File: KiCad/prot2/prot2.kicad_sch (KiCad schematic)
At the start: 1 part, among them Q1 Q_Photo_NPN

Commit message: 回路図仮完成
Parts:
- added C1, C10, C2, C3, C4, C5, C6, C7, C8, C9: C, symbol Device:C
- added C11, C12, C13: C_Polarized_Small_US, symbol Device:C_Polarized_Small_US
- added D1, D10, D11, D12, D13, D14, D15, D16, D17, D18, D19, D2, D20, D21, D22, D23, D24, D25, D26, D27, D28, D29, D3, D30, D31, D32, D4, D5, D6, D7, D8, D9: LED, symbol Device:LED
- added D33: D_Schottky, symbol Device:D_Schottky
- added J1: Conn_01x02_Socket, symbol Connector:Conn_01x02_Socket
- added J2: LED_SW, symbol Connector_Generic:Conn_01x03
- added J3: Conn_01x04_Socket, symbol Connector:Conn_01x04_Socket
- added Q10, Q11, Q12, Q13, Q14, Q15, Q16, Q17, Q18, Q19, Q2, Q20, Q21, Q22, Q23, Q24, Q25, Q26, Q27, Q28, Q29, Q3, Q30, Q31, Q32, Q4, Q5, Q6, Q7, Q8, Q9: Q_Photo_NPN, symbol Device:Q_Photo_NPN
- added RP2040_Zero1, RP2040_Zero2: ~, RP2040_Zero:名称未設定, symbol RP2040-zero:RP2040_Zero
- added RV1: R_Potentiometer_Trim, symbol Device:R_Potentiometer_Trim
- added Rc1, Rc10, Rc11, Rc12, Rc13, Rc14, Rc15, Rc16, Rc17, Rc18, Rc19, Rc2, Rc20, Rc21, Rc22, Rc23, Rc24, Rc25, Rc26, Rc27, Rc28, Rc29, Rc3, Rc30, Rc31, Rc32, Rc4, Rc5, Rc6, Rc7, Rc8, Rc9, Rl1, Rl10, Rl11, Rl12, Rl13, Rl14, Rl15, Rl16, Rl17, Rl18, Rl19, Rl2, Rl20, Rl21, Rl22, Rl23, Rl24, Rl25, Rl26, Rl27, Rl28, Rl29, Rl3, Rl30, Rl31, Rl32, Rl4, Rl5, Rl6, Rl7, Rl8, Rl9, Rs1, Rs10, Rs11, Rs12, Rs13, Rs14, Rs15, Rs16, Rs17, Rs18, Rs19, Rs2, Rs20, Rs21, Rs22, Rs23, Rs24, Rs25, Rs26, Rs27, Rs28, Rs29, Rs3, Rs30, Rs31, Rs32, Rs4, Rs5, Rs6, Rs7, Rs8, Rs9: R, symbol Device:R
- added U1, U2, U3, U4, U5, U6, U7, U8: LM339, symbol Comparator:LM339
- Q1: footprint ALS-PT19-315C:ALS-PT19-315C -> (none)
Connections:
- net VCC: now reaches Q1.1 (C)
- net VCC: now also C1.1, C2.1, C3.1, C4.1, C5.1, C6.1, C7.1, C8.1, D33.1 (K), Q10.1 (C), Q11.1 (C), Q12.1 (C), Q13.1 (C), Q14.1 (C), Q15.1 (C), Q16.1 (C), Q17.1 (C), Q18.1 (C), Q19.1 (C), Q2.1 (C), Q20.1 (C), Q21.1 (C), Q22.1 (C), Q23.1 (C), Q24.1 (C), Q25.1 (C), Q26.1 (C), Q27.1 (C), Q28.1 (C), Q29.1 (C), Q3.1 (C), Q30.1 (C), Q31.1 (C), Q32.1 (C), Q4.1 (C), Q5.1 (C), Q6.1 (C), Q7.1 (C), Q8.1 (C), Q9.1 (C), RP2040_Zero1.21 (3V3), RP2040_Zero2.21 (3V3), RV1.1, Rc1.1, Rc10.1, Rc11.1, Rc12.1, Rc13.1, Rc14.1, Rc15.1, Rc16.1, Rc17.1, Rc18.1, Rc19.1, Rc2.1, Rc20.1, Rc21.1, Rc22.1, Rc23.1, Rc24.1, Rc25.1, Rc26.1, Rc27.1, Rc28.1, Rc29.1, Rc3.1, Rc30.1, Rc31.1, Rc32.1, Rc4.1, Rc5.1, Rc6.1, Rc7.1, Rc8.1, Rc9.1, U1.3 (V+), U2.3 (V+), U3.3 (V+), U4.3 (V+), U5.3 (V+), U6.3 (V+), U7.3 (V+), U8.3 (V+)
- net at Q1.2 (E): now also Rs1.1, U1.4 (-)
- new net: Q4.2 (E), Rs4.1, U1.8 (-)
- new net: Q16.2 (E), Rs16.1, U4.8 (-)
- new net: D27.1 (K), Rl27.1
- new net: D12.1 (K), Rl12.1
- new net: D32.1 (K), Rl32.1
- new net: Q7.2 (E), Rs7.1, U2.10 (-)
- new net: D24.1 (K), Rl24.1
- new net: Q32.2 (E), Rs32.1, U8.8 (-)
- new net: Q31.2 (E), Rs31.1, U7.8 (-)
- new net: D3.1 (K), Rl3.1
- new net: Q14.2 (E), Rs14.1, U4.6 (-)
- new net: D28.1 (K), Rl28.1
- new net: D4.1 (K), Rl4.1
- new net: D30.1 (K), Rl30.1
- new net: Q27.2 (E), Rs27.1, U7.10 (-)
- new net: Q13.2 (E), Rs13.1, U4.4 (-)
- new net: Q12.2 (E), Rs12.1, U3.8 (-)
- new net: Q29.2 (E), Rs29.1, U5.8 (-)
- new net: D9.1 (K), Rl9.1
- new net: D14.1 (K), Rl14.1
- new net: Q8.2 (E), Rs8.1, U2.8 (-)
- new net: Q10.2 (E), Rs10.1, U3.6 (-)
- new net: D7.1 (K), Rl7.1
- new net: Q5.2 (E), Rs5.1, U2.4 (-)
- new net: Q9.2 (E), Rs9.1, U3.4 (-)
- new net: Q23.2 (E), Rs23.1, U7.6 (-)
- new net: D17.1 (K), Rl17.1
- new net: D18.1 (K), Rl18.1
- new net: Q19.2 (E), Rs19.1, U7.4 (-)
- new net: D11.1 (K), Rl11.1
- new net: Q24.2 (E), Rs24.1, U8.6 (-)
- new net: Q22.2 (E), Rs22.1, U6.6 (-)
- new net: Q3.2 (E), Rs3.1, U1.10 (-)
- new net: D31.1 (K), Rl31.1
- new net: D25.1 (K), Rl25.1
- new net: Q2.2 (E), Rs2.1, U1.6 (-)
- new net: D10.1 (K), Rl10.1
- new net: D8.1 (K), Rl8.1
- new net: D21.1 (K), Rl21.1
- new net: D16.1 (K), Rl16.1
- new net: D6.1 (K), Rl6.1
- new net: Q11.2 (E), Rs11.1, U3.10 (-)
- new net: Q21.2 (E), Rs21.1, U5.6 (-)
- new net: Q26.2 (E), Rs26.1, U6.10 (-)
- new net: Q20.2 (E), Rs20.1, U8.4 (-)
- new net: RP2040_Zero1., RP2040_Zero1.8 (7)
- new net: Q15.2 (E), Rs15.1, U4.10 (-)
- new net: D13.1 (K), Rl13.1
- new net: D19.1 (K), Rl19.1
- new net: Q18.2 (E), Rs18.1, U6.4 (-)
- new net: D22.1 (K), Rl22.1
- new net: Q6.2 (E), Rs6.1, U2.6 (-)
- new net: D26.1 (K), Rl26.1
- new net: D15.1 (K), Rl15.1
- new net: Q30.2 (E), Rs30.1, U6.8 (-)
- new net: Q25.2 (E), Rs25.1, U5.10 (-)
- new net: Q17.2 (E), Rs17.1, U5.4 (-)
- new net: Q28.2 (E), Rs28.1, U8.10 (-)
- new net: D1.1 (K), Rl1.1
- new net: D23.1 (K), Rl23.1
- new net: D2.1 (K), Rl2.1
- new net: D29.1 (K), Rl29.1
- new net: RP2040_Zero2., RP2040_Zero2.8 (7)
- new net: D20.1 (K), Rl20.1
- new net: D5.1 (K), Rl5.1
- new net 1: Rc1.2, U1.2
- new net 10: Rc10.2, U3.1
- new net 11: Rc11.2, U3.13
- new net 12: Rc12.2, U3.14
- new net 13: Rc13.2, U4.2
- new net 14: Rc14.2, U4.1
- new net 15: Rc15.2, U4.13
- new net 16: Rc16.2, U4.14
- new net 17: Rc17.2, U5.2
- new net 18: Rc18.2, U5.1
- new net 19: Rc19.2, U5.13
- new net 2: Rc2.2, U1.1
- new net 20: Rc20.2, U5.14
- new net 21: Rc21.2, U6.2
- new net 22: Rc22.2, U6.1
- new net 23: Rc23.2, U6.13
- new net 24: Rc24.2, U6.14
- new net 25: Rc25.2, U7.2
- new net 26: Rc26.2, U7.1
- new net 27: Rc27.2, U7.13
- new net 28: Rc28.2, U7.14
- new net 29: Rc29.2, U8.2
- new net 3: Rc3.2, U1.13
- new net 30: Rc30.2, U8.1
- new net 31: Rc31.2, U8.13
- new net 32: Rc32.2, U8.14
- new net 4: Rc4.2, U1.14
- new net 5: Rc5.2, U2.2
- new net 6: Rc6.2, U2.1
- new net 7: Rc7.2, U2.13
- new net 8: Rc8.2, U2.14
- new net 9: Rc9.2, U3.2
- new net GND: C1.2, C2.2, C3.2, C4.2, C5.2, C6.2, C7.2, C8.2, RP2040_Zero1.22 (GND), RP2040_Zero2.22 (GND), RV1.3, Rl1.2, Rl10.2, Rl11.2, Rl12.2, Rl13.2, Rl14.2, Rl15.2, Rl16.2, Rl17.2, Rl18.2, Rl19.2, Rl2.2, Rl20.2, Rl21.2, Rl22.2, Rl23.2, Rl24.2, Rl25.2, Rl26.2, Rl27.2, Rl28.2, Rl29.2, Rl3.2, Rl30.2, Rl31.2, Rl32.2, Rl4.2, Rl5.2, Rl6.2, Rl7.2, Rl8.2, Rl9.2, Rs1.2, Rs10.2, Rs11.2, Rs12.2, Rs13.2, Rs14.2, Rs15.2, Rs16.2, Rs17.2, Rs18.2, Rs19.2, Rs2.2, Rs20.2, Rs21.2, Rs22.2, Rs23.2, Rs24.2, Rs25.2, Rs26.2, Rs27.2, Rs28.2, Rs29.2, Rs3.2, Rs30.2, Rs31.2, Rs32.2, Rs4.2, Rs5.2, Rs6.2, Rs7.2, Rs8.2, Rs9.2, U1.12 (V-), U2.12 (V-), U3.12 (V-), U4.12 (V-), U5.12 (V-), U6.12 (V-), U7.12 (V-), U8.12 (V-)
- new net LED_5V: D1.2 (A), D10.2 (A), D11.2 (A), D12.2 (A), D13.2 (A), D14.2 (A), D15.2 (A), D16.2 (A), D17.2 (A), D18.2 (A), D19.2 (A), D2.2 (A), D20.2 (A), D21.2 (A), D22.2 (A), D23.2 (A), D24.2 (A), D25.2 (A), D26.2 (A), D27.2 (A), D28.2 (A), D29.2 (A), D3.2 (A), D30.2 (A), D31.2 (A), D32.2 (A), D4.2 (A), D5.2 (A), D6.2 (A), D7.2 (A), D8.2 (A), D9.2 (A), J2.3 (Pin_3)
- new net conp_+: RV1.2, U1.11 (+), U1.5 (+), U1.7 (+), U1.9 (+), U2.11 (+), U2.5 (+), U2.7 (+), U2.9 (+), U3.11 (+), U3.5 (+), U3.7 (+), U3.9 (+), U4.11 (+), U4.5 (+), U4.7 (+), U4.9 (+), U5.11 (+), U5.5 (+), U5.7 (+), U5.9 (+), U6.11 (+), U6.5 (+), U6.7 (+), U6.9 (+), U7.11 (+), U7.5 (+), U7.7 (+), U7.9 (+), U8.11 (+), U8.5 (+), U8.7 (+), U8.9 (+)
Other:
- note added: "LED_POWER"
- note added: "UART"

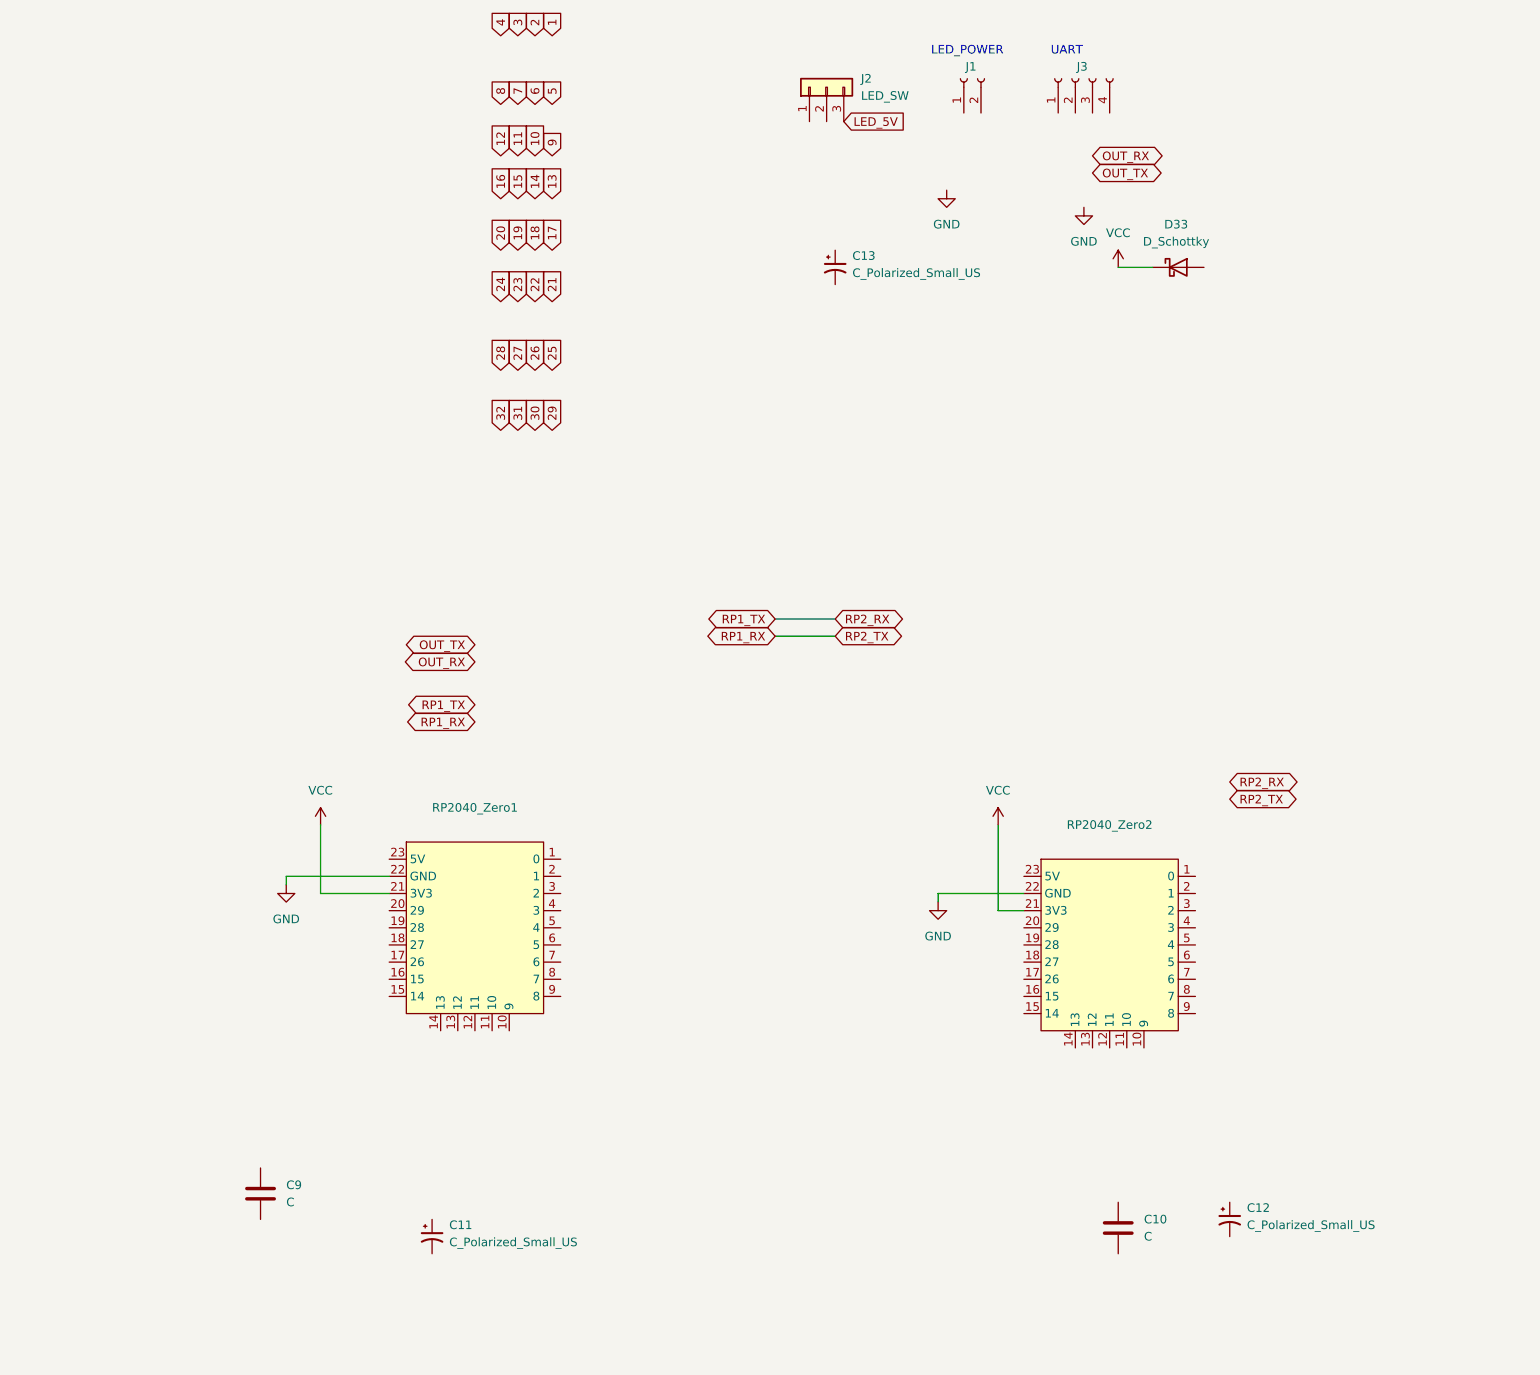
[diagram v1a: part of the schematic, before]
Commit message: フットプイリント割当完了
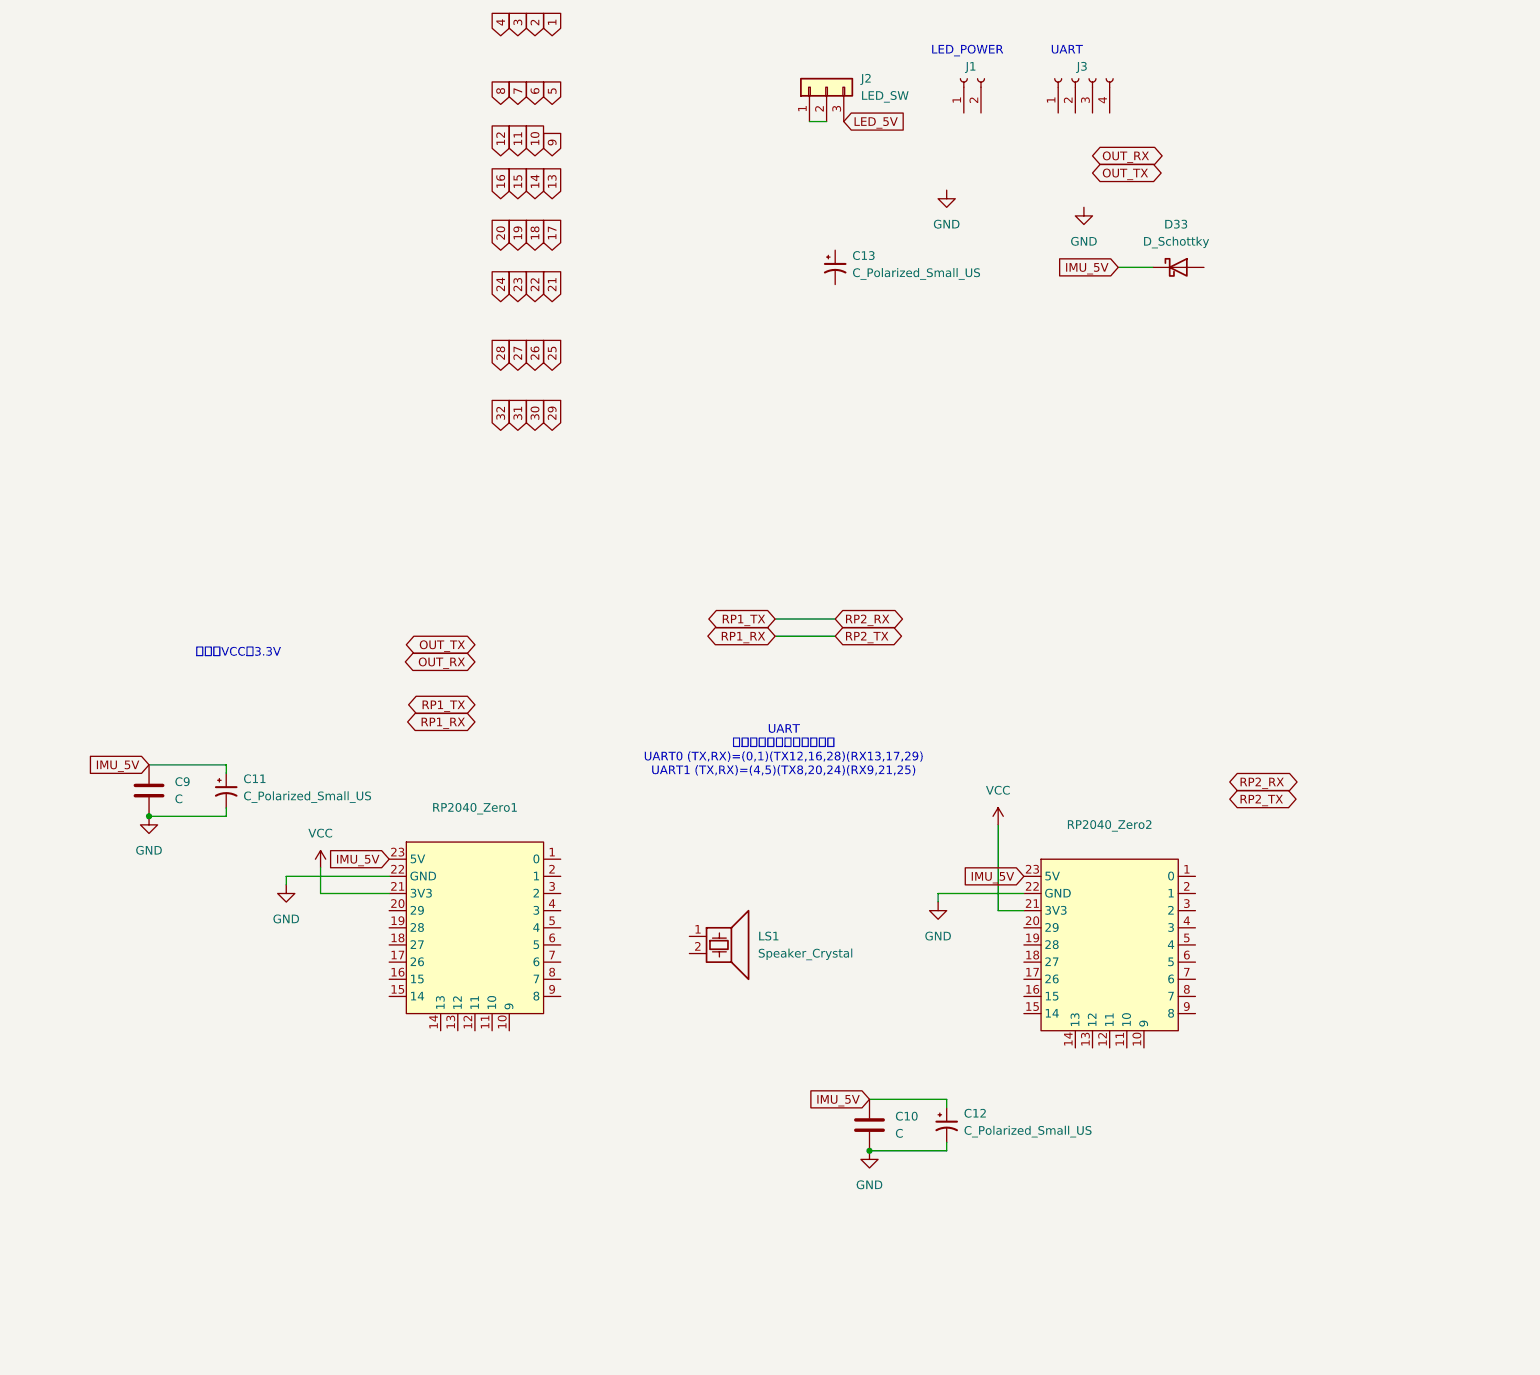
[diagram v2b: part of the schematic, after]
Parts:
- added LS1: Speaker_Crystal, Buzzer_Beeper:Buzzer_TDK_PS1240P02BT_D12.2mm_H6.5mm, symbol Device:Speaker_Crystal
- C1, C10, C2, C3, C4, C5, C6, C7, C8, C9: footprint (none) -> Capacitor_SMD:C_0603_1608Metric_Pad1.08x0.95mm_HandSolder
- C11, U1, U2, U3, U4, U5, U6, U7, U8: footprint (none) -> Package_SO:SOIC-14_3.9x8.7mm_P1.27mm
- C12, C13: footprint (none) -> Capacitor_THT:C_Radial_D8.0mm_H11.5mm_P3.50mm
- D1, D10, D11, D12, D13, D14, D15, D16, D17, D18, D19, D2, D20, D21, D22, D23, D24, D25, D26, D27, D28, D29, D3, D30, D31, D32, D4, D5, D6, D7, D8, D9: footprint (none) -> LED_SMD:LED_0603_1608Metric_Pad1.05x0.95mm_HandSolder
- D33: footprint (none) -> Diode_SMD:D_SOD-323_HandSoldering
- J1: footprint (none) -> Connector_JST:JST_XH_S2B-XH-A_1x02_P2.50mm_Horizontal
- J2: footprint (none) -> Connector_PinHeader_2.54mm:PinHeader_1x03_P2.54mm_Vertical
- J3: footprint (none) -> Connector_JST:JST_PH_S4B-PH-K_1x04_P2.00mm_Horizontal
- Q1, RV1: footprint (none) -> hankotei:hankotei_node
- Q10, Q11, Q12, Q13, Q14, Q15, Q16, Q17, Q18, Q19, Q2, Q20, Q21, Q22, Q23, Q24, Q25, Q26, Q27, Q28, Q29, Q3, Q30, Q31, Q32, Q4, Q5, Q6, Q7, Q8, Q9: footprint (none) -> NJL7502R:NJL7502R
- RP2040_Zero1, RP2040_Zero2: footprint RP2040_Zero:名称未設定 -> RP2040zero:RP2040_zero
- Rc1, Rc10, Rc11, Rc12, Rc13, Rc14, Rc15, Rc16, Rc17, Rc18, Rc19, Rc2, Rc20, Rc21, Rc22, Rc23, Rc24, Rc25, Rc26, Rc27, Rc28, Rc29, Rc3, Rc30, Rc31, Rc32, Rc4, Rc5, Rc6, Rc7, Rc8, Rc9, Rl1, Rl10, Rl11, Rl12, Rl13, Rl14, Rl15, Rl16, Rl17, Rl18, Rl19, Rl2, Rl20, Rl21, Rl22, Rl23, Rl24, Rl25, Rl26, Rl27, Rl28, Rl29, Rl3, Rl30, Rl31, Rl32, Rl4, Rl5, Rl6, Rl7, Rl8, Rl9, Rs1, Rs10, Rs11, Rs12, Rs13, Rs14, Rs15, Rs16, Rs17, Rs18, Rs19, Rs2, Rs20, Rs21, Rs22, Rs23, Rs24, Rs25, Rs26, Rs27, Rs28, Rs29, Rs3, Rs30, Rs31, Rs32, Rs4, Rs5, Rs6, Rs7, Rs8, Rs9: footprint (none) -> Resistor_SMD:R_0603_1608Metric_Pad0.98x0.95mm_HandSolder
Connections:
- net GND: now also C10.2, C11.2, C12.2, C9.2
- net VCC: no longer D33.1 (K)
- net IMU_5V: now reaches C11.1
- net IMU_5V: now also C10.1, C12.1, C9.1, D33.1 (K), RP2040_Zero1.23 (5V), RP2040_Zero2.23 (5V)
- net at J2.1 (Pin_1): now also J2.2 (Pin_2)
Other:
- note added: "UART ハードウェアシリアルなら UART0 (TX,RX)=(0,1)(TX12,16,28)(RX13,17,29) UART1 (TX,RX)=(4,5)(TX8,20,24)(RX9,21,25)"
- note added: "注意：VCCは3.3V"
- moved on the sheet: C11, C9

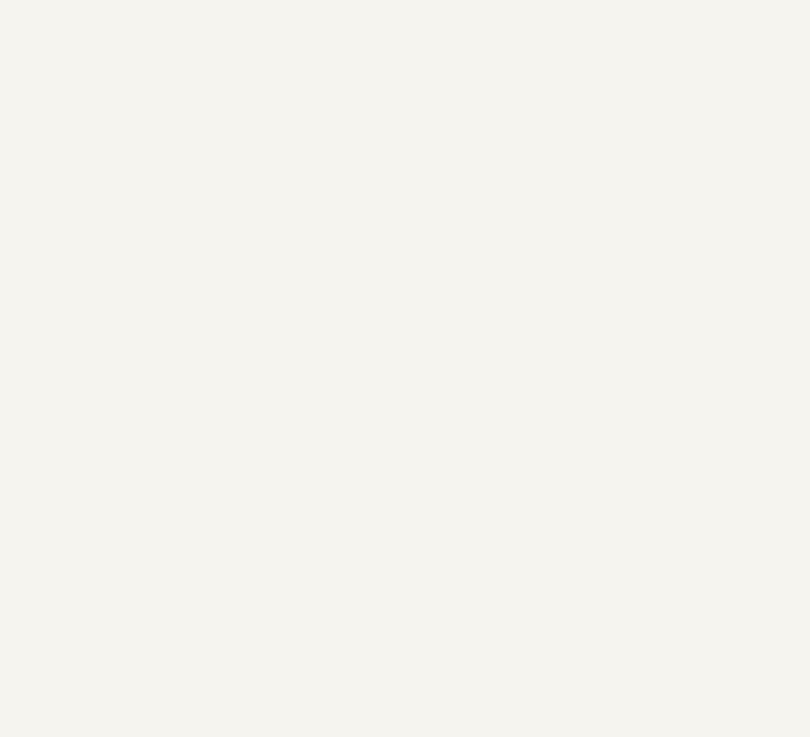
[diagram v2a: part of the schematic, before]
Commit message: ネジ穴配置
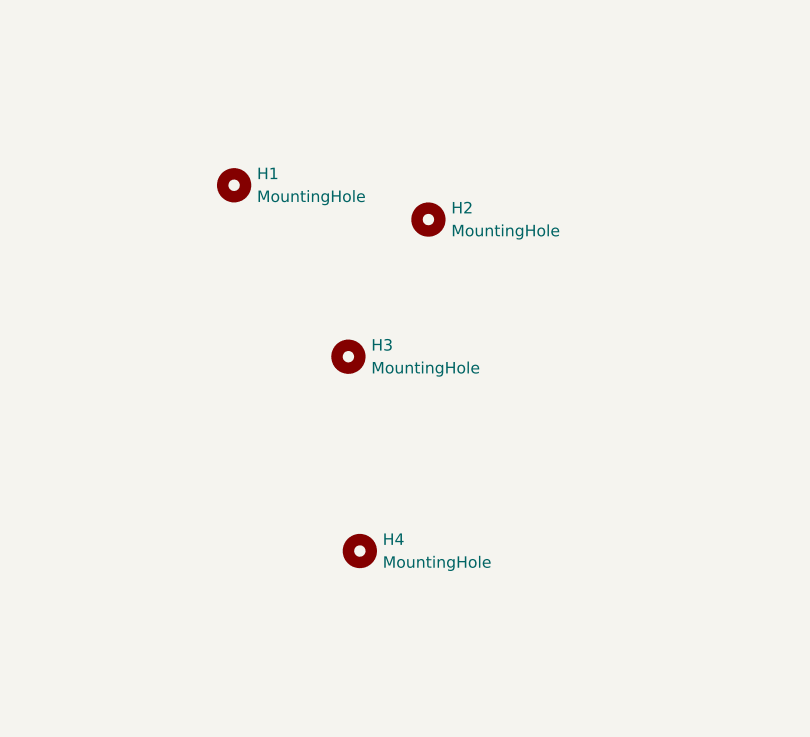
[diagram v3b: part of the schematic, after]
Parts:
- added H1, H2, H3, H4: MountingHole, MountingHole:MountingHole_3.2mm_M3, symbol Mechanical:MountingHole
